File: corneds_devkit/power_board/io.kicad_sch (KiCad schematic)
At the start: 2 parts, among them J1 Conn_01x07_Female, J2 Conn_01x07_Female

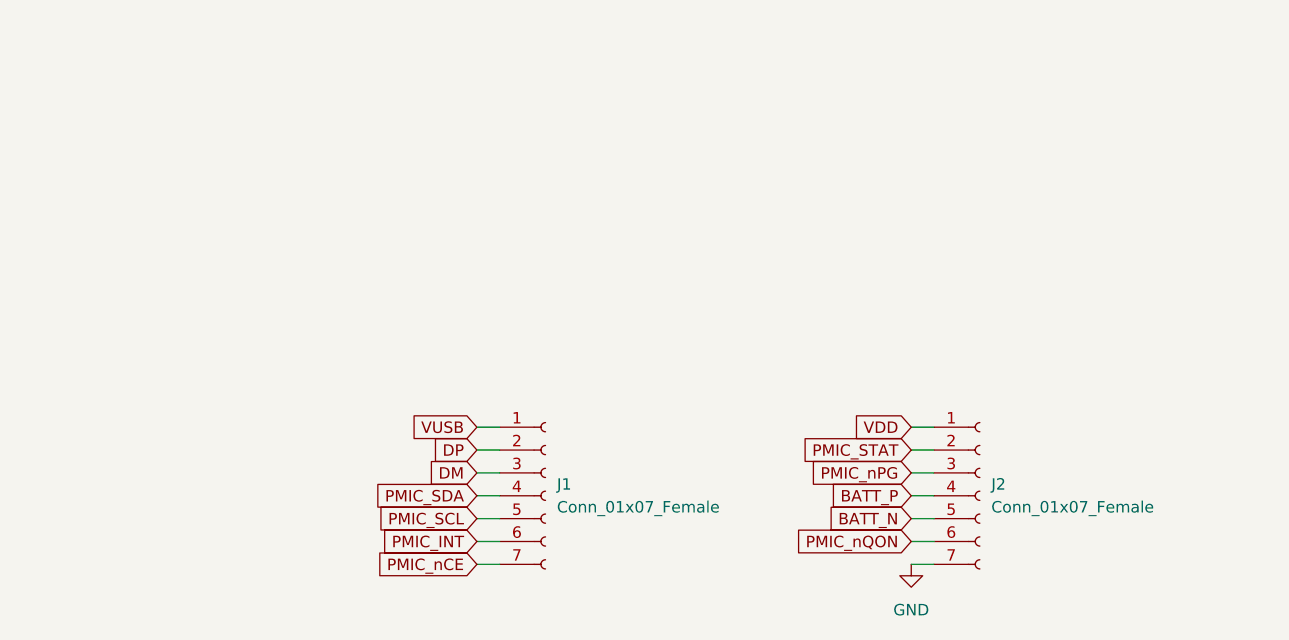
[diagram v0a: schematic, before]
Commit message: made power schematic and started on routing power board
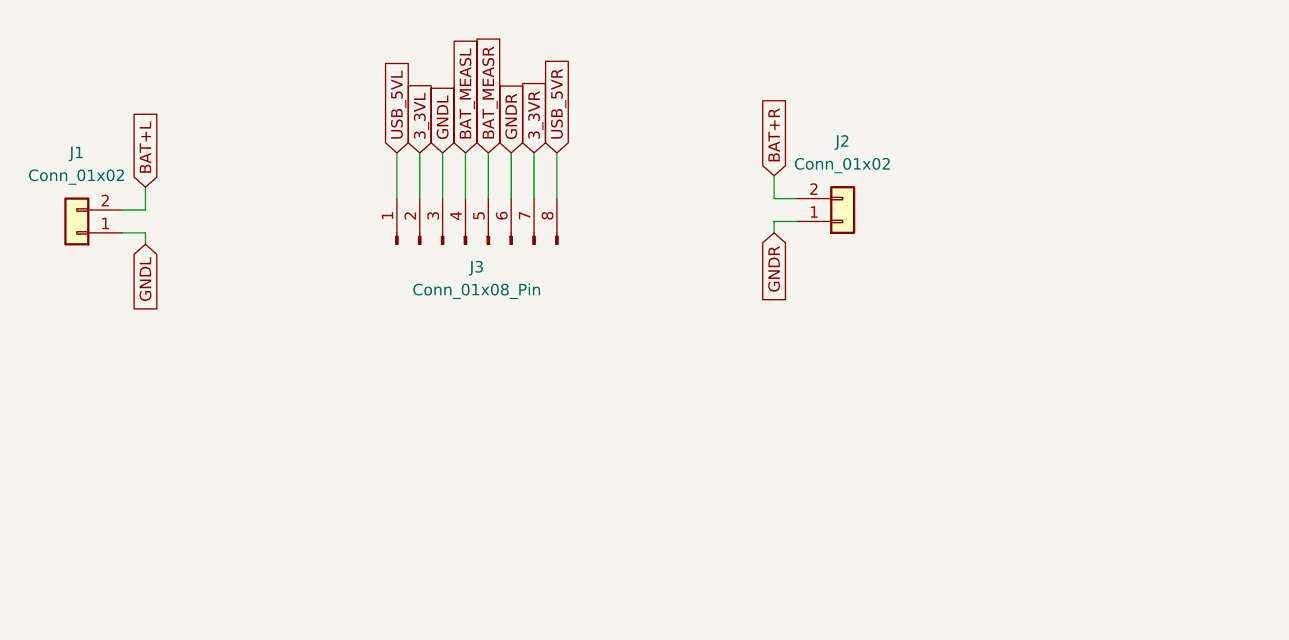
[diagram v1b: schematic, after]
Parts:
- removed J1, J2: Conn_01x07_Female, symbol Connector:Conn_01x07_Female
- added J1, J2: Conn_01x02, Connector_JST:JST_PH_S2B-PH-K_1x02_P2.00mm_Horizontal, symbol Connector_Generic:Conn_01x02
- added J3: Conn_01x08_Pin, Connector_PinHeader_1.27mm:PinHeader_1x08_P1.27mm_Horizontal, symbol Connector:Conn_01x08_Pin
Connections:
- new net 3_3VL: J3.2 (Pin_2)
- new net 3_3VR: J3.7 (Pin_7)
- new net BAT+L: J1.2 (Pin_2)
- new net BAT+R: J2.2 (Pin_2)
- new net BAT_MEASL: J3.4 (Pin_4)
- new net BAT_MEASR: J3.5 (Pin_5)
- new net GNDL: J1.1 (Pin_1), J3.3 (Pin_3)
- new net GNDR: J2.1 (Pin_1), J3.6 (Pin_6)
- new net USB_5VL: J3.1 (Pin_1)
- new net USB_5VR: J3.8 (Pin_8)

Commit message: finished routing power board and started on control board schematic but realized I need seperate reset lines
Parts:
- J3: footprint Connector_PinHeader_1.27mm:PinHeader_1x08_P1.27mm_Horizontal -> Connector_PinHeader_1.27mm:PinHeader_1x08_P1.27mm_Vertical
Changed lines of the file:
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@@
 			)
 		)
-		(property "Footprint" "Connector_PinHeader_1.27mm:PinHeader_1x08_P1.27mm_Horizontal"
+		(property "Footprint" "Connector_PinHeader_1.27mm:PinHeader_1x08_P1.27mm_Vertical"
 			(at 95.25 50.8 0)
 			(effects

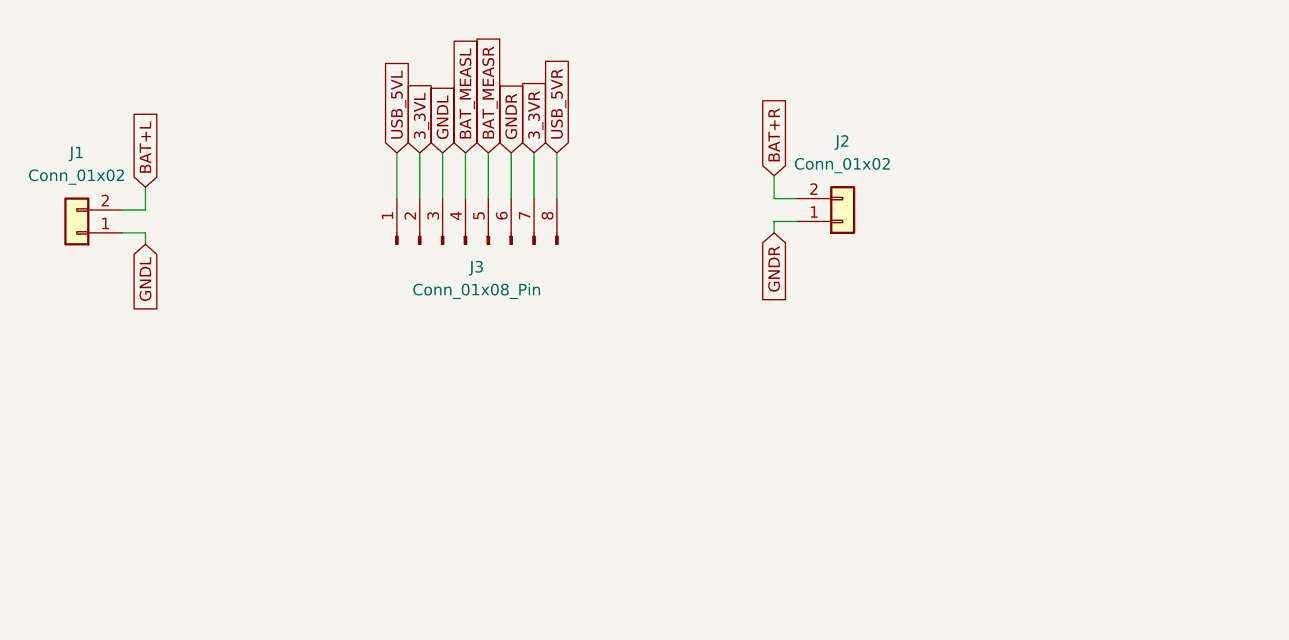
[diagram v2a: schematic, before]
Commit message: ordered devkit rev A
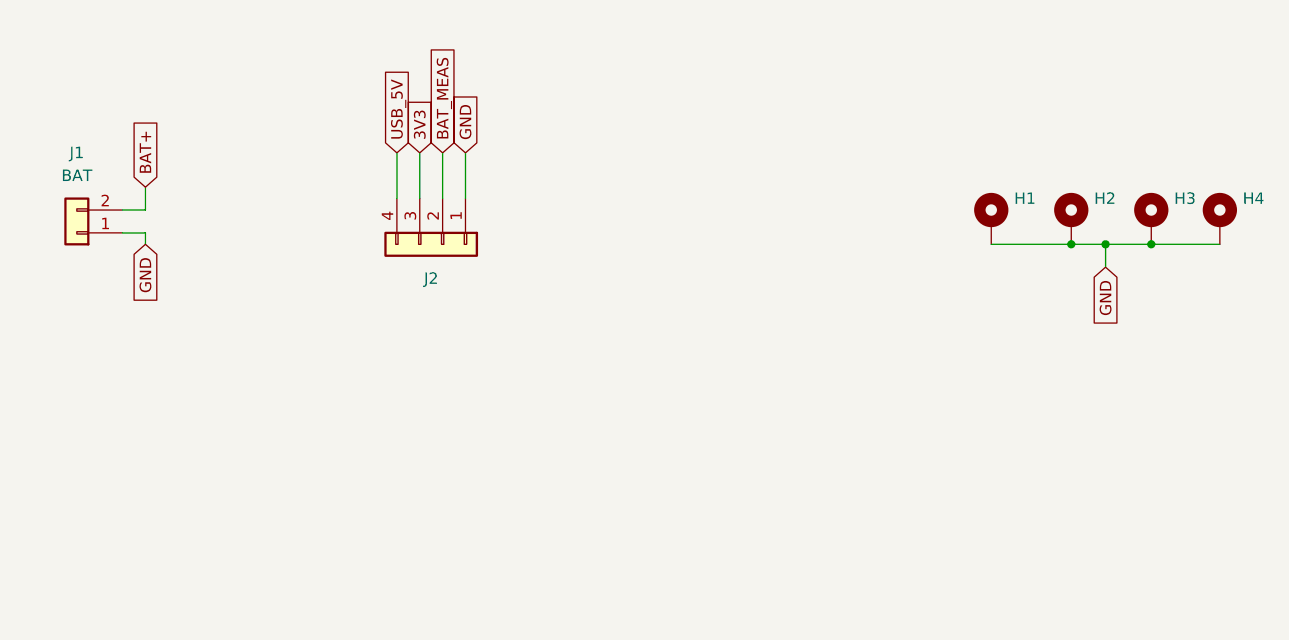
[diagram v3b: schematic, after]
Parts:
- removed J2: Conn_01x02, Connector_JST:JST_PH_S2B-PH-K_1x02_P2.00mm_Horizontal, symbol Connector_Generic:Conn_01x02
- removed J3: Conn_01x08_Pin, Connector_PinHeader_1.27mm:PinHeader_1x08_P1.27mm_Vertical, symbol Connector:Conn_01x08_Pin
- added H1, H2, H3, H4: ~, MountingHole:MountingHole_3.2mm_M3_Pad_Via, symbol Mechanical:MountingHole_Pad
- added J2: ~, Connector_PinHeader_1.27mm:PinHeader_1x04_P1.27mm_Vertical, symbol Connector_Generic:Conn_01x04
- J1: value Conn_01x02 -> BAT
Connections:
- net BAT+L renamed BAT+
- net GNDL renamed GND
- net GND: now also H1.1, H2.1, H3.1, H4.1, J2.1 (Pin_1)
- new net 3V3: J2.3 (Pin_3)
- new net BAT_MEAS: J2.2 (Pin_2)
- new net USB_5V: J2.4 (Pin_4)
